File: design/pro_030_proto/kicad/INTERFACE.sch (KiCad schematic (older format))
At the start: 3 parts, among them IC30 PCF8584, J24 I2C

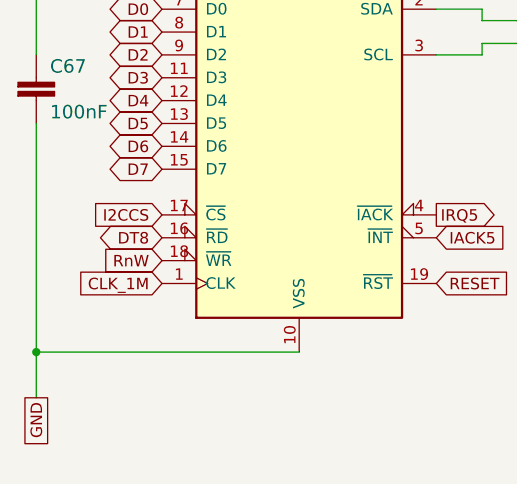
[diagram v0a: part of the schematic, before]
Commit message: Reconnect PCF8584 clock to CLK_8M
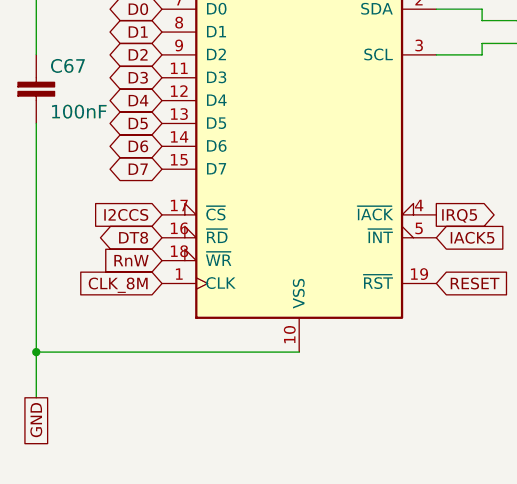
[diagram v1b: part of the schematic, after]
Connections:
- net CLK_1M renamed CLK_8M
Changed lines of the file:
@@
 I2CCS
 Text GLabel 5700 4450 0    50   Input ~ 0
-CLK_1M
+CLK_8M
 $Comp
 L Connector:Conn_01x02_Male J24

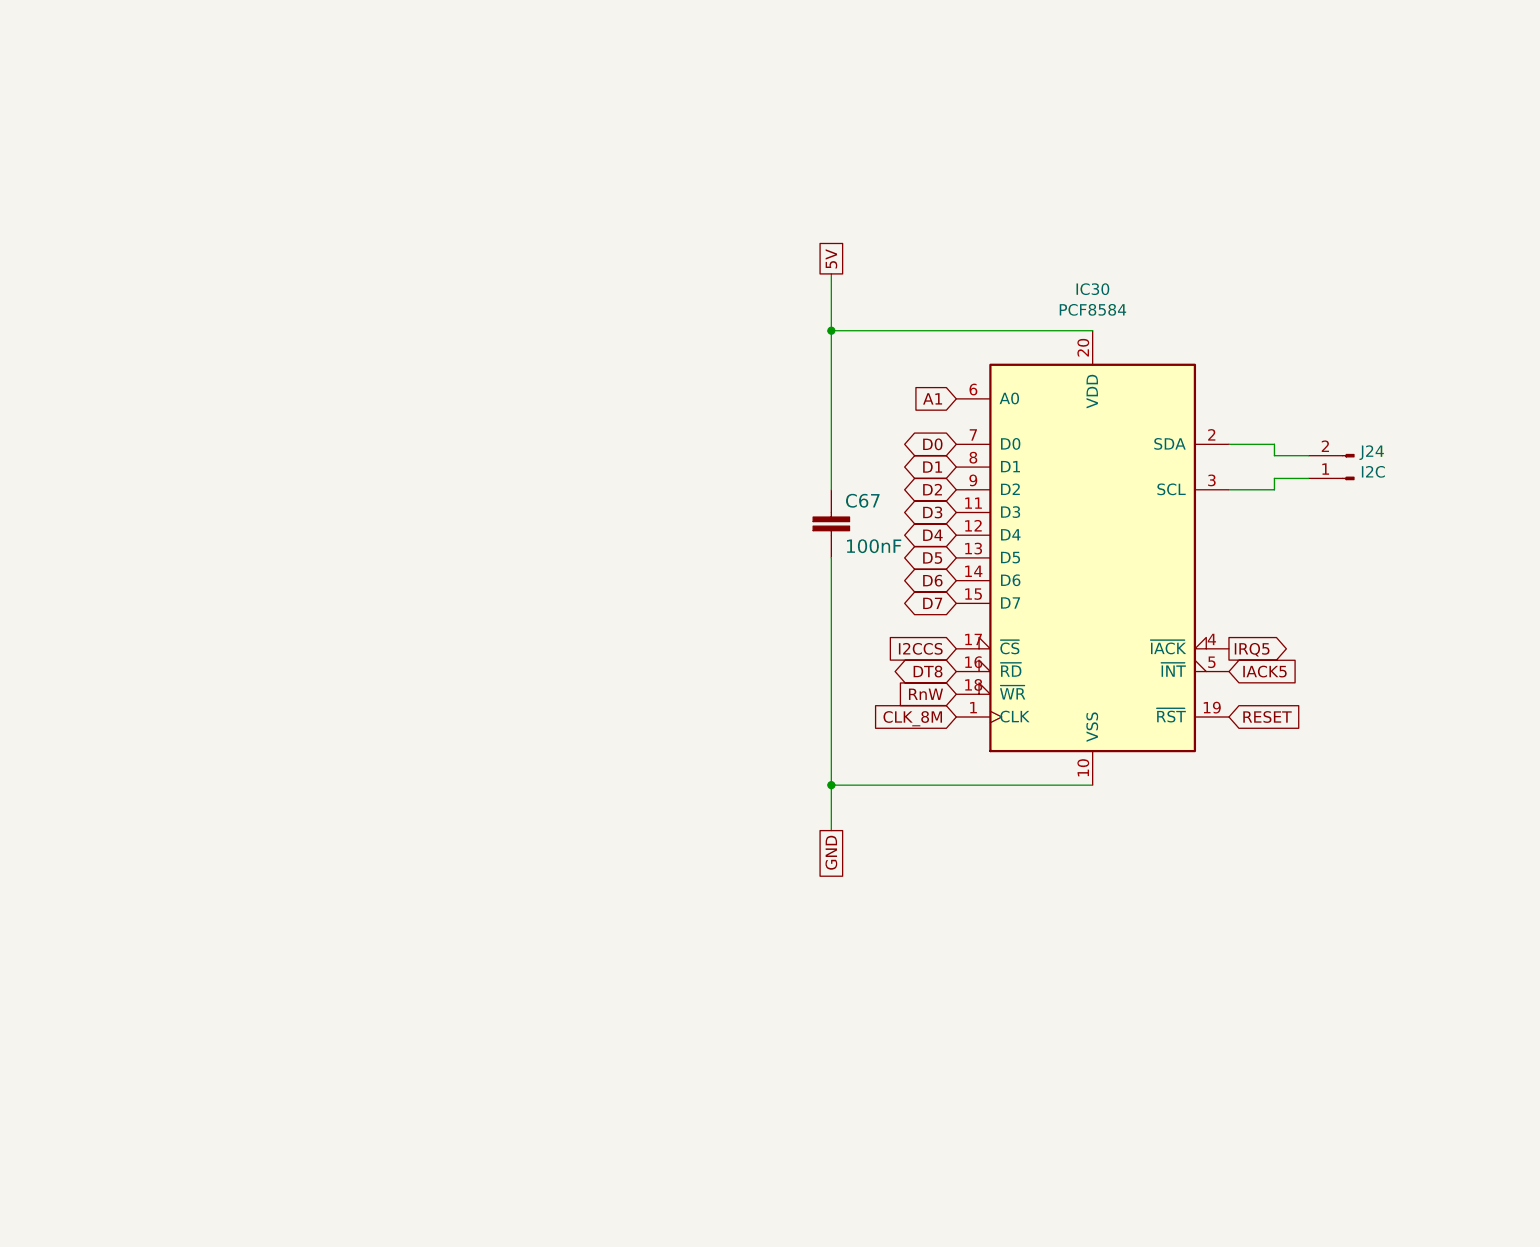
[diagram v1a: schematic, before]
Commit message: Lots more changes
* Add DIN expansion connectors (provisional pinout)
* Fix incorrect address lines for RAM & ROM (Doh!)
* Remove unused level shifters
* Fix clock enables
* Lots of other small fixes
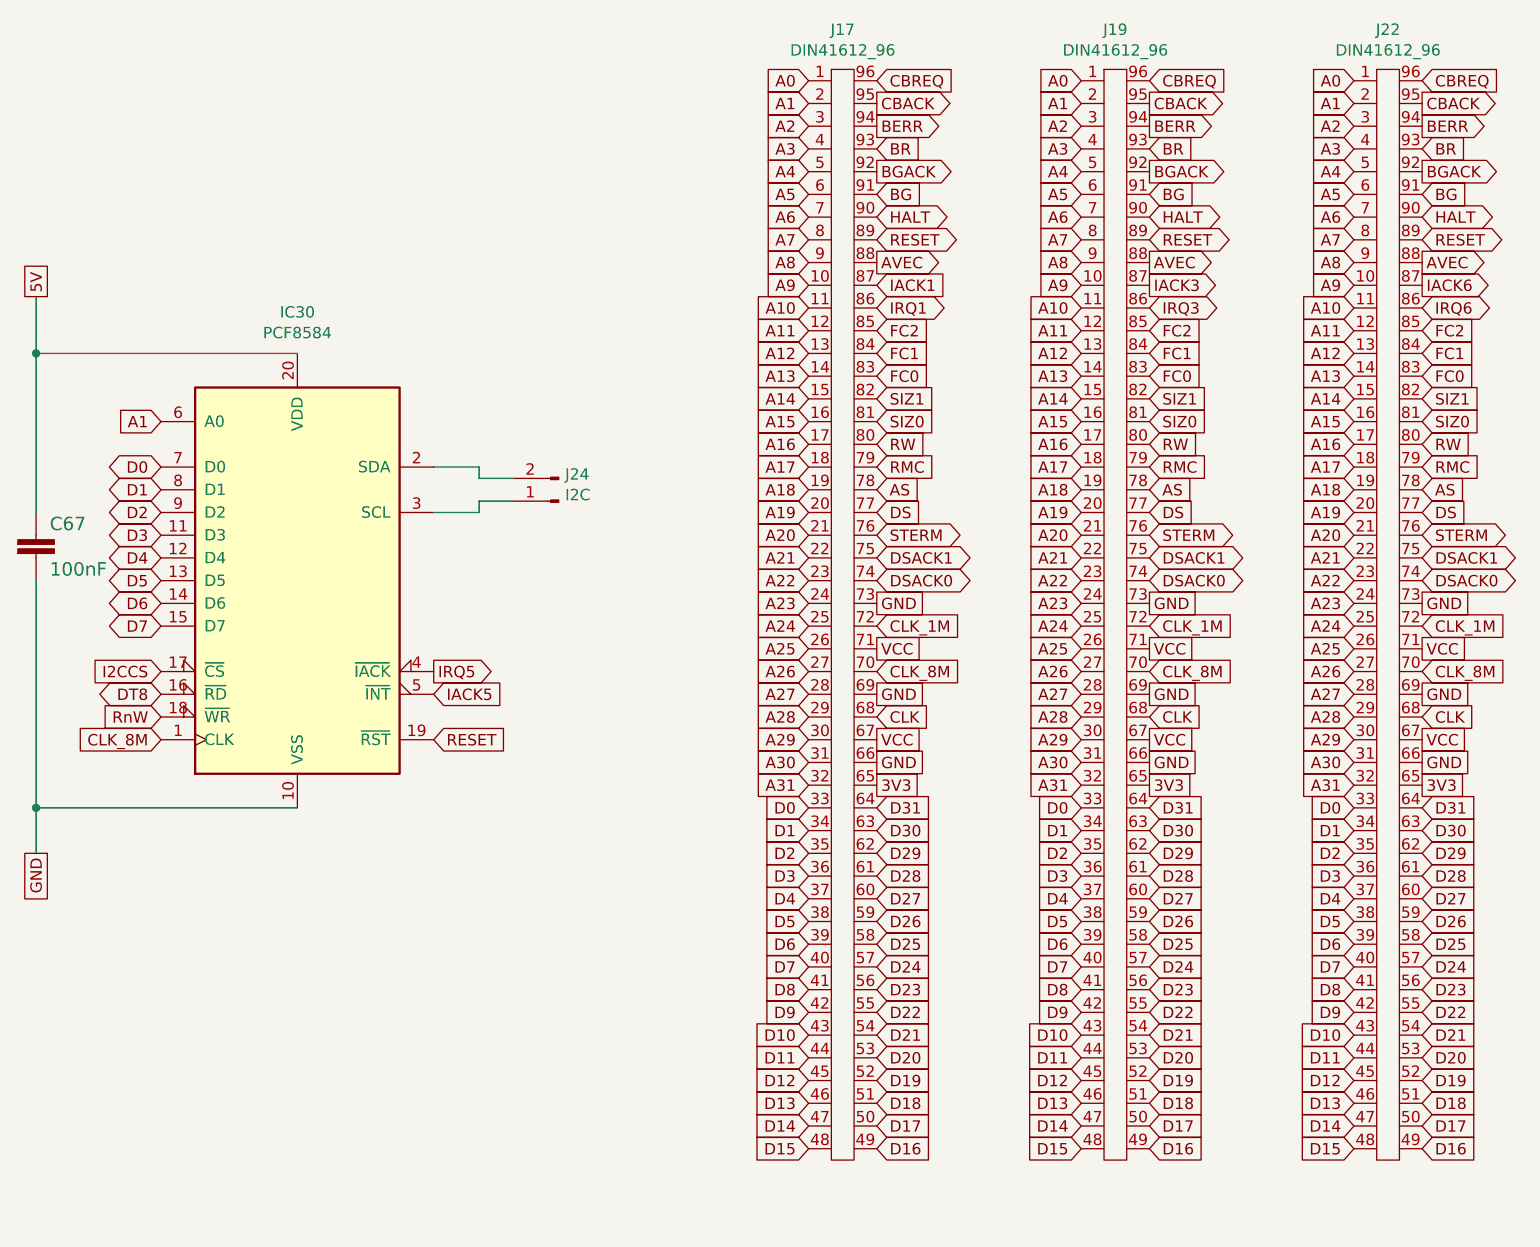
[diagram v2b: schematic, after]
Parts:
- added J17, J19, J22: DIN41612_96, rosco_m68k:DIN41612_B_3x32_Vertical, symbol rosco_m68k:DIN41612_96
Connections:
- net A1: now also J17.2, J19.2, J22.2
- net CLK_8M: now also J17.70, J19.70, J22.70
- net D0: now also J17.33, J19.33, J22.33
- net D1: now also J17.34, J19.34, J22.34
- net D2: now also J17.35, J19.35, J22.35
- net D3: now also J17.36, J19.36, J22.36
- net D4: now also J17.37, J19.37, J22.37
- net D5: now also J17.38, J19.38, J22.38
- net D6: now also J17.39, J19.39, J22.39
- net D7: now also J17.40, J19.40, J22.40
- net GND: now also J17.66, J17.69, J17.73, J19.66, J19.69, J19.73, J22.66, J22.69, J22.73
- net RESET: now also J17.89, J19.89, J22.89
- new net 3V3: J17.65, J19.65, J22.65
- new net A0: J17.1, J19.1, J22.1
- new net A10: J17.11, J19.11, J22.11
- new net A11: J17.12, J19.12, J22.12
- new net A12: J17.13, J19.13, J22.13
- new net A13: J17.14, J19.14, J22.14
- new net A14: J17.15, J19.15, J22.15
- new net A15: J17.16, J19.16, J22.16
- new net A16: J17.17, J19.17, J22.17
- new net A17: J17.18, J19.18, J22.18
- new net A18: J17.19, J19.19, J22.19
- new net A19: J17.20, J19.20, J22.20
- new net A2: J17.3, J19.3, J22.3
- new net A20: J17.21, J19.21, J22.21
- new net A21: J17.22, J19.22, J22.22
- new net A22: J17.23, J19.23, J22.23
- new net A23: J17.24, J19.24, J22.24
- new net A24: J17.25, J19.25, J22.25
- new net A25: J17.26, J19.26, J22.26
- new net A26: J17.27, J19.27, J22.27
- new net A27: J17.28, J19.28, J22.28
- new net A28: J17.29, J19.29, J22.29
- new net A29: J17.30, J19.30, J22.30
- new net A3: J17.4, J19.4, J22.4
- new net A30: J17.31, J19.31, J22.31
- new net A31: J17.32, J19.32, J22.32
- new net A4: J17.5, J19.5, J22.5
- new net A5: J17.6, J19.6, J22.6
- new net A6: J17.7, J19.7, J22.7
- new net A7: J17.8, J19.8, J22.8
- new net A8: J17.9, J19.9, J22.9
- new net A9: J17.10, J19.10, J22.10
- new net AS: J17.78, J19.78, J22.78
- new net AVEC: J17.88, J19.88, J22.88
- new net BERR: J17.94, J19.94, J22.94
- new net BG: J17.91, J19.91, J22.91
- new net BGACK: J17.92, J19.92, J22.92
- new net BR: J17.93, J19.93, J22.93
- new net CBACK: J17.95, J19.95, J22.95
- new net CBREQ: J17.96, J19.96, J22.96
- new net CLK: J17.68, J19.68, J22.68
- new net CLK_1M: J17.72, J19.72, J22.72
- new net D10: J17.43, J19.43, J22.43
- new net D11: J17.44, J19.44, J22.44
- new net D12: J17.45, J19.45, J22.45
- new net D13: J17.46, J19.46, J22.46
- new net D14: J17.47, J19.47, J22.47
- new net D15: J17.48, J19.48, J22.48
- new net D16: J17.49, J19.49, J22.49
- new net D17: J17.50, J19.50, J22.50
- new net D18: J17.51, J19.51, J22.51
- new net D19: J17.52, J19.52, J22.52
- new net D20: J17.53, J19.53, J22.53
- new net D21: J17.54, J19.54, J22.54
- new net D22: J17.55, J19.55, J22.55
- new net D23: J17.56, J19.56, J22.56
- new net D24: J17.57, J19.57, J22.57
- new net D25: J17.58, J19.58, J22.58
- new net D26: J17.59, J19.59, J22.59
- new net D27: J17.60, J19.60, J22.60
- new net D28: J17.61, J19.61, J22.61
- new net D29: J17.62, J19.62, J22.62
- new net D30: J17.63, J19.63, J22.63
- new net D31: J17.64, J19.64, J22.64
- new net D8: J17.41, J19.41, J22.41
- new net D9: J17.42, J19.42, J22.42
- new net DS: J17.77, J19.77, J22.77
- new net DSACK0: J17.74, J19.74, J22.74
- new net DSACK1: J17.75, J19.75, J22.75
- new net FC0: J17.83, J19.83, J22.83
- new net FC1: J17.84, J19.84, J22.84
- new net FC2: J17.85, J19.85, J22.85
- new net HALT: J17.90, J19.90, J22.90
- new net IACK1: J17.87
- new net IACK3: J19.87
- new net IACK6: J22.87
- new net IRQ1: J17.86
- new net IRQ3: J19.86
- new net IRQ6: J22.86
- new net RMC: J17.79, J19.79, J22.79
- new net RW: J17.80, J19.80, J22.80
- new net SIZ0: J17.81, J19.81, J22.81
- new net SIZ1: J17.82, J19.82, J22.82
- new net STERM: J17.76, J19.76, J22.76
- new net VCC: J17.67, J17.71, J19.67, J19.71, J22.67, J22.71
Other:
- moved on the sheet: C67, IC30, J24

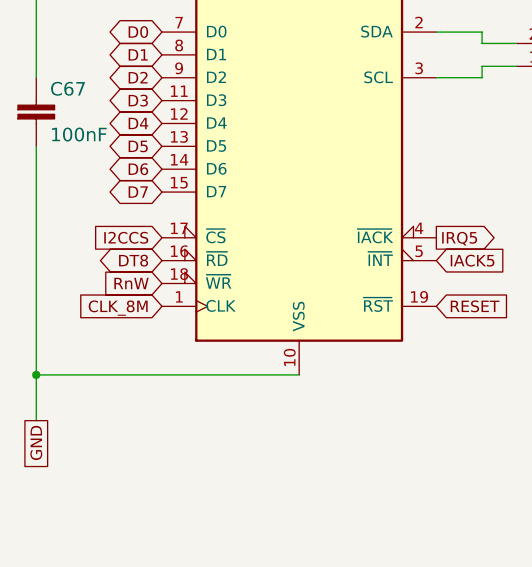
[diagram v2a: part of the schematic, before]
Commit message: Fix RW/RnW SNAFU
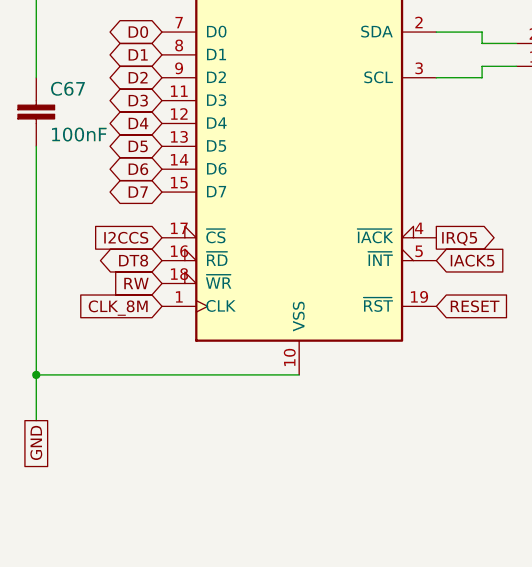
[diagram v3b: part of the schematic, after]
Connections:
- net RnW is gone; now on net RW: IC30.18 (~WR~)
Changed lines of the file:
@@
 DT8
 Text GLabel 2200 4450 0    50   Input ~ 0
-RnW
+RW
 Text GLabel 3400 4250 2    50   Output ~ 0
 IRQ5

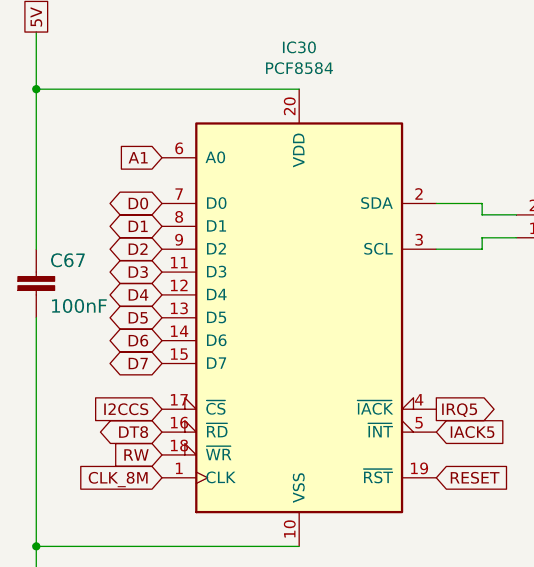
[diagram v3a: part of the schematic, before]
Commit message: Fix (another) hilarious mistake 😞
* 8-bit ports wired to the wrong end of the bus
* Another respin needed I think...
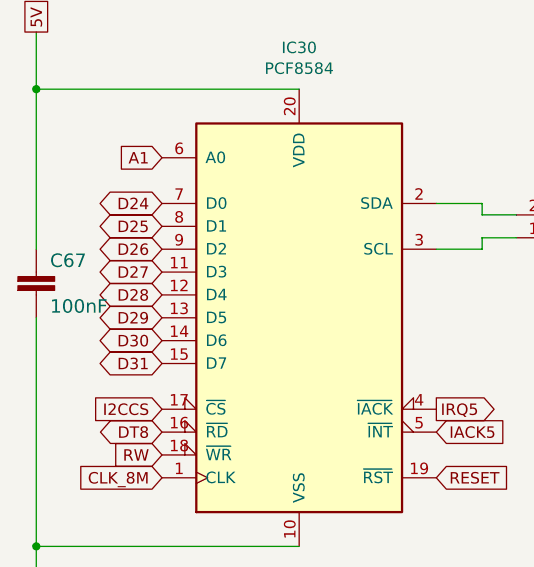
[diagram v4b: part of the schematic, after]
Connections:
- net D0: no longer IC30.7 (D0)
- net D1: no longer IC30.8 (D1)
- net D2: no longer IC30.9 (D2)
- net D24: now also IC30.7 (D0)
- net D25: now also IC30.8 (D1)
- net D26: now also IC30.9 (D2)
- net D27: now also IC30.11 (D3)
- net D28: now also IC30.12 (D4)
- net D29: now also IC30.13 (D5)
- net D3: no longer IC30.11 (D3)
- net D30: now also IC30.14 (D6)
- net D31: now also IC30.15 (D7)
- net D4: no longer IC30.12 (D4)
- net D5: no longer IC30.13 (D5)
- net D6: no longer IC30.14 (D6)
- net D7: no longer IC30.15 (D7)
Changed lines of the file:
@@
 A1
 Text GLabel 2200 3350 0    50   3State ~ 0
-D0
+D24
 Text GLabel 2200 3450 0    50   3State ~ 0
-D1
+D25
 Text GLabel 2200 3550 0    50   3State ~ 0
-D2
+D26
 Text GLabel 2200 3650 0    50   3State ~ 0
-D3
+D27
 Text GLabel 2200 3750 0    50   3State ~ 0
-D4
+D28
 Text GLabel 2200 3850 0    50   3State ~ 0
-D5
+D29
 Text GLabel 2200 3950 0    50   3State ~ 0
-D6
+D30
 Text GLabel 2200 4050 0    50   3State ~ 0
-D7
+D31
 Text GLabel 2200 4350 0    50   3State ~ 0
 DT8

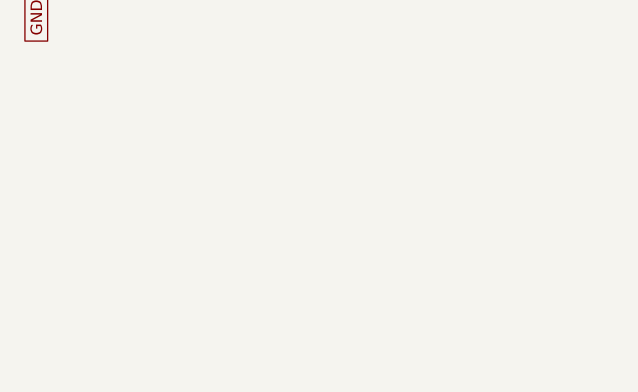
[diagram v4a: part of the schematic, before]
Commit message: Add legacy SD / SPI header
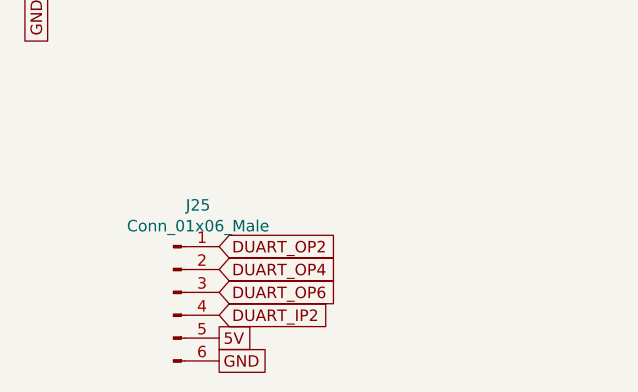
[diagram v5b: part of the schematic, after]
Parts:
- added J25: Conn_01x06_Male, Connector_PinHeader_2.54mm:PinHeader_1x06_P2.54mm_Vertical, symbol Connector:Conn_01x06_Male
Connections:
- net 5V: now also J25.5 (Pin_5)
- net GND: now also J25.6 (Pin_6)
- new net DUART_IP2: J25.4 (Pin_4)
- new net DUART_OP2: J25.1 (Pin_1)
- new net DUART_OP4: J25.2 (Pin_2)
- new net DUART_OP6: J25.3 (Pin_3)
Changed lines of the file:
@@
 Text GLabel 7750 4650 2    50   UnSpc ~ 0
 GND
+$Comp
+L Connector:Conn_01x06_Male J?
+U 1 1 61A9011E
+P 2250 6350
+AR Path="/60FBD3A8/61A9011E" Ref="J?"  Part="1"
+AR Path="/61738494/61A9011E" Ref="J25"  Part="1"
+F 0 "J25" H 2358 6731 50  0000 C CNN
+F 1 "Conn_01x06_Male" H 2358 6640 50  0000 C CNN
+F 2 "Connector_PinHeader_2.54mm:PinHeader_1x06_P2.54mm_Vertical" H 2250 6350 50  0001 C CNN
+F 3 "~" H 2250 6350 50  0001 C CNN
+	1    2250 6350
+	1    0    0    -1
+$EndComp
+Text GLabel 2450 6150 2    50   Input ~ 0
+DUART_OP2
+Text GLabel 2450 6250 2    50   Input ~ 0
+DUART_OP4
+Text GLabel 2450 6350 2    50   Input ~ 0
+DUART_OP6
+Text GLabel 2450 6450 2    50   Input ~ 0
+DUART_IP2
+Text GLabel 2450 6550 2    50   UnSpc ~ 0
+5V
+Text GLabel 2450 6650 2    50   UnSpc ~ 0
+GND
 $EndSCHEMATC
